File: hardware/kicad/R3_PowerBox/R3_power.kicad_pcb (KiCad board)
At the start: 4 copper layers, 160 x 80 mm, 199 parts, among them J1 SERVICE / BENCH INPUT 6-12V, J10 BATTERY / CHARGER TELEMETRY, J11 USER PANEL / PRIMARY ONLY, J12 PRIMARY B2B 2x8 / DNP, J13 ISOLATED B2B 2x5 / DNP, J2 DIGITAL POWER OUT, J3 ISOLATED POWER OUT, J4 CONTROL / SERVICE, J5 PRIMARY AUX DNP, J6 ISOLATED AUX DNP, J7 USB-C POWER INPUT, J8 2S BATTERY / KEYED / NTC_BMS=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, J9 NTC_CHG=103AT-2 / QUIET DGND 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, Q1 DMP3007LSS-13, Q2 CSD17577Q3AT 30V NMOS DSG, Q3 CSD17577Q3AT 30V NMOS CHG, Q4 DMP3007LSS-13 SYSTEM LOAD SWI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, SW1 C&K RS282G05A3 / POWER ON, SW2 QON SERVICE / TL3305AF160QG, U1 TPS62132RGTR, U10 STUSB4500QTR, U11 BQ294502 SPACE ONLY / NC / DNP, U2 TPS54302DDCR, U3 RS3E-0505S/H3, U4 ADM7150ACPZ-3.3-R7, U5 TPS7A2033PDBVR, U6 RS3-0505D/H3, U7 TPS2121RUXR, U8 BQ25798RQM, U9 BQ28Z610DRZR

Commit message: Route R3 checkpoint E domain planes and thermal returns
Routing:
- net VSYS_MAIN: track 103.1 -> 106.4 mm, vias 5 -> 8
- net GND_ISO: track 24.3 -> 27.3 mm, vias 22 -> 31
- net VSYS_PROT: track 27.9 -> 30.2 mm, vias 3 -> 5
- net DGND: vias 67 -> 85
- added copper zone on B.Cu, net BMS_FET_COMMON
- added copper zone on F.Cu, net BMS_FET_COMMON
- added copper zone on B.Cu, net DGND
- added copper zone on F.Cu, net DGND
- added copper zone on In1.Cu, net DGND
- added copper zone on In2.Cu, net DGND
- added copper zone on B.Cu, net GND_ISO
- added copper zone on F.Cu, net GND_ISO
- added copper zone on In1.Cu, net GND_ISO
- added copper zone on In2.Cu, net GND_ISO
- added copper zone on B.Cu, net VSYS_MAIN
- added copper zone on F.Cu, net VSYS_MAIN
- added copper zone on B.Cu, net VSYS_PROT
- added copper zone on F.Cu, net VSYS_PROT

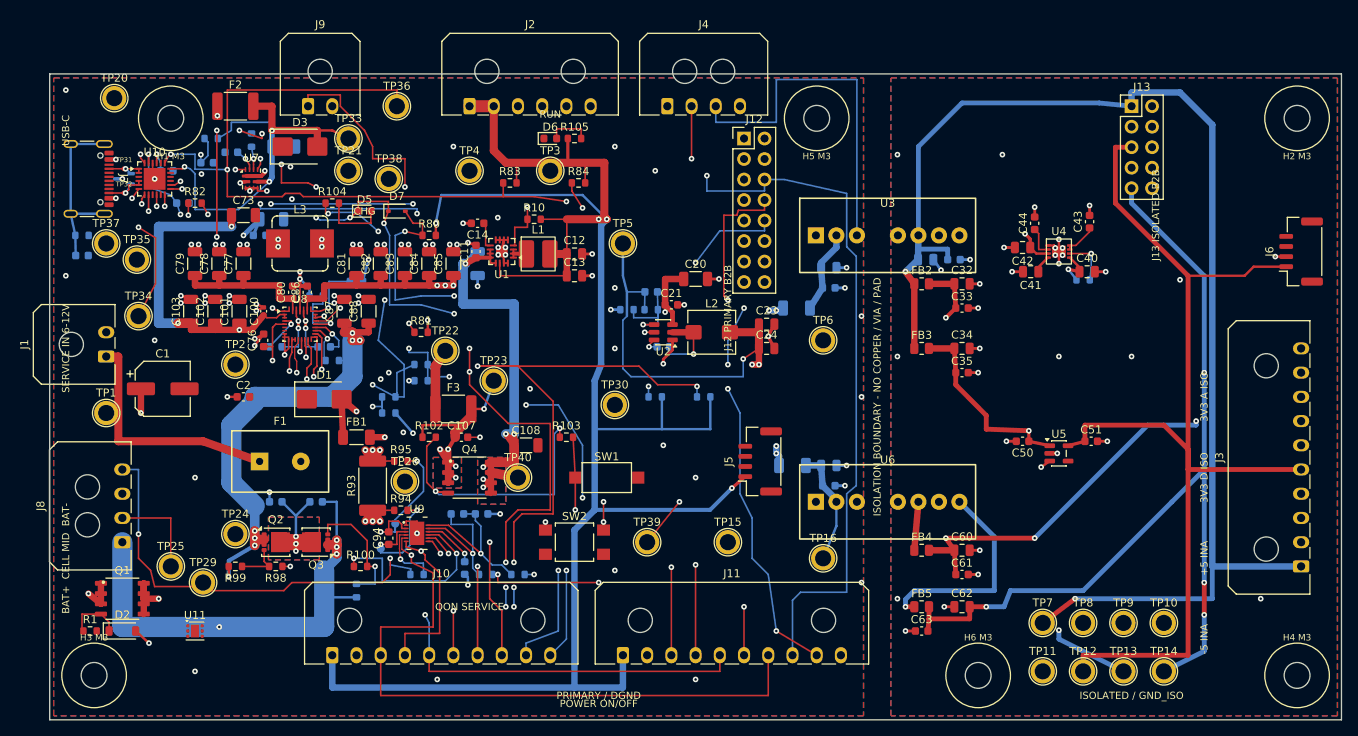
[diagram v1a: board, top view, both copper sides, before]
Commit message: Finish R3 PowerBox routing checkpoint F and verification
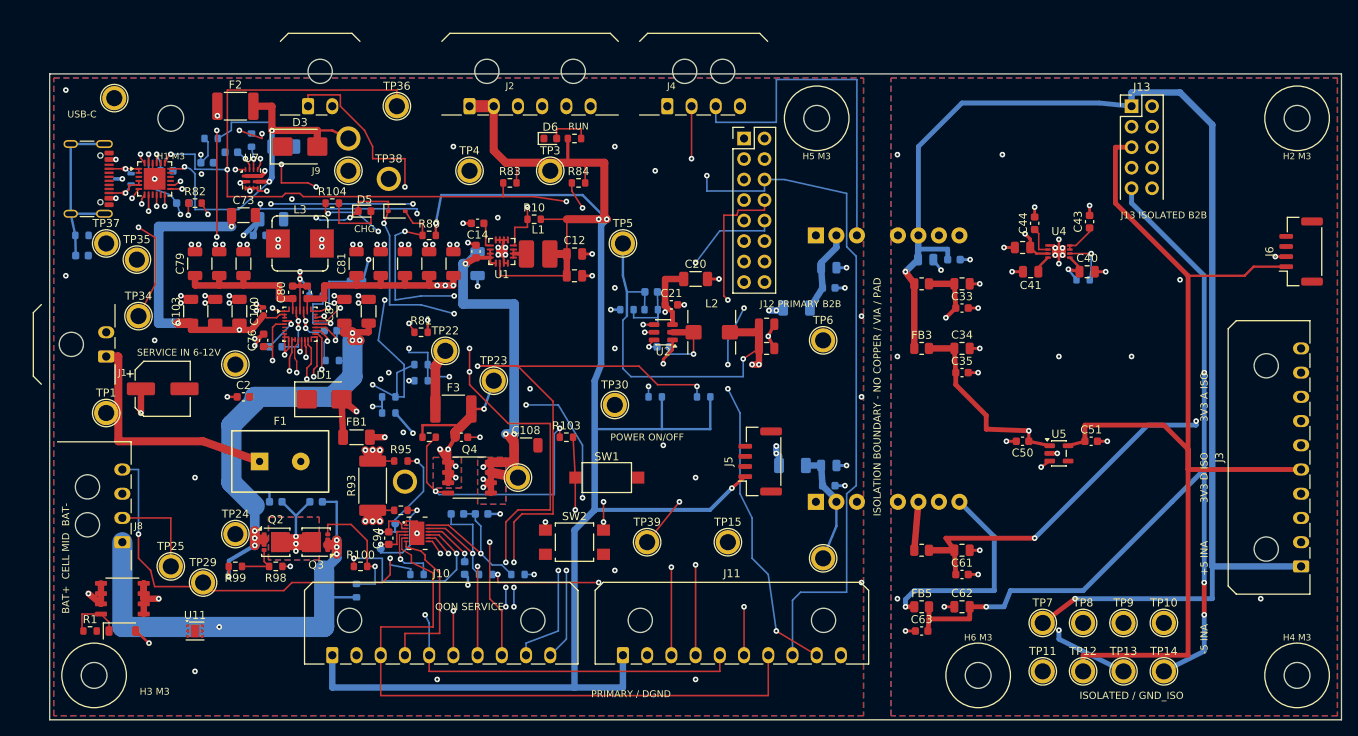
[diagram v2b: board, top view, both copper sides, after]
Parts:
- C1: footprint CP_Elec_6.3x5.8 -> Capacitor_SMD:CP_Elec_6.3x5.8
- C10, C101, C102, C103, C108, C20, C3, C71, C73, C77, C78, C79, C81, C82, C83, C84, C85, C87, C88: footprint C_1206_3216Metric -> Capacitor_SMD:C_1206_3216Metric
- C100: footprint C_0402_1005Metric -> Capacitor_SMD:C_0402_1005Metric
- C104, C105, C106, C107, C11, C14, C2, C21, C22, C25, C27, C29, C31, C33, C35, C4, C43, C44, C50, C51, C61, C63, C70, C72, C74, C75, C76, C80, C86, C89, C93, C94, C95, C96, C97, C98: footprint C_0603_1608Metric -> Capacitor_SMD:C_0603_1608Metric
- C12, C13, C23, C24, C26, C28, C30, C32, C34, C40, C41, C42, C60, C62: footprint C_0805_2012Metric -> Capacitor_SMD:C_0805_2012Metric
- D1, D3: footprint D_SMB -> Diode_SMD:D_SMB
- D2: footprint D_SOD-123 -> Diode_SMD:D_SOD-123
- D4: footprint SOT-323_SC-70 -> Package_TO_SOT_SMD:SOT-323_SC-70
- D5, D6: footprint LED_0603_1608Metric -> LED_SMD:LED_0603_1608Metric
- D7: footprint D_SOD-323 -> Diode_SMD:D_SOD-323
- F1: footprint Fuse_PTC_MF-R250 -> R3_Power:Fuse_PTC_MF-R250
- F2, F3: footprint Fuse_1812_4532Metric_Pad1.30x3.40mm_HandSolder -> Fuse:Fuse_1812_4532Metric_Pad1.30x3.40mm_HandSolder
- FB1, FB6, FB7: footprint L_1206_3216Metric_Pad1.22x1.90mm_HandSolder -> Inductor_SMD:L_1206_3216Metric_Pad1.22x1.90mm_HandSolder
- FB2, FB3, FB4, FB5: footprint R_0805_2012Metric -> Resistor_SMD:R_0805_2012Metric
- J1, J9: footprint Molex_Micro-Fit_3.0_43650-0200_1x02_P3.00mm_Horizontal -> Connector_Molex:Molex_Micro-Fit_3.0_43650-0200_1x02_P3.00mm_Horizontal
- J10, J11, J3: footprint Molex_Micro-Fit_3.0_43650-1000_1x10_P3.00mm_Horizontal -> Connector_Molex:Molex_Micro-Fit_3.0_43650-1000_1x10_P3.00mm_Horizontal
- J12: footprint PinHeader_2x08_P2.54mm_Vertical -> Connector_PinHeader_2.54mm:PinHeader_2x08_P2.54mm_Vertical
- J13: footprint PinHeader_2x05_P2.54mm_Vertical -> Connector_PinHeader_2.54mm:PinHeader_2x05_P2.54mm_Vertical
- J2: footprint Molex_Micro-Fit_3.0_43650-0600_1x06_P3.00mm_Horizontal -> Connector_Molex:Molex_Micro-Fit_3.0_43650-0600_1x06_P3.00mm_Horizontal
- J4, J8: footprint Molex_Micro-Fit_3.0_43650-0400_1x04_P3.00mm_Horizontal -> Connector_Molex:Molex_Micro-Fit_3.0_43650-0400_1x04_P3.00mm_Horizontal
- J5, J6: footprint JST_GH_SM04B-GHS-TB_1x04-1MP_P1.25mm_Horizontal -> Connector_JST:JST_GH_SM04B-GHS-TB_1x04-1MP_P1.25mm_Horizontal
- J7: footprint USB_C_Receptacle_GCT_USB4105-xx-A_16P_TopMnt_Horizontal -> Connector_USB:USB_C_Receptacle_GCT_USB4105-xx-A_16P_TopMnt_Horizontal
- L1: footprint L_Coilcraft_XFL4020 -> R3_Power:L_Coilcraft_XFL4020
- L2: footprint L_Bourns_SRP5030T -> Inductor_SMD:L_Bourns_SRP5030T
- L3: value 1.0uH >=6A / MPN TBD -> SRP7028A-1R0M 1uH; footprint L_Bourns_SRP7028A_7.3x6.6mm -> Inductor_SMD:L_Bourns_SRP7028A_7.3x6.6mm
- Q1, Q4: footprint DMP3007LSS_SO8_LOGICAL -> R3_Power:DMP3007LSS_SO8_LOGICAL
- Q2, Q3: footprint CSD17577Q3A_VSON-8_3.3x3.3mm -> R3_Power:CSD17577Q3A_VSON-8_3.3x3.3mm
- R1, R10, R100, R101, R102, R103, R104, R105, R21, R22, R40, R72, R73, R74, R75, R76, R77, R78, R79, R80, R81, R82, R83, R84, R85, R90, R91, R92, R94, R95, R96, R97, R98, R99: footprint R_0603_1608Metric -> Resistor_SMD:R_0603_1608Metric
- R93: footprint R_2512_6332Metric_Pad1.40x3.35mm_HandSolder -> Resistor_SMD:R_2512_6332Metric_Pad1.40x3.35mm_HandSolder
- SW1: footprint SW_SPST_CK_RS282G05A3 -> Button_Switch_SMD:SW_SPST_CK_RS282G05A3
- SW2: footprint SW_SPST_TL3305A -> Button_Switch_SMD:SW_SPST_TL3305A
- TP1, TP10, TP11, TP12, TP13, TP14, TP15, TP16, TP2, TP20, TP21, TP22, TP23, TP24, TP25, TP26, TP29, TP3, TP30, TP33, TP34, TP35, TP36, TP37, TP38, TP39, TP4, TP40, TP5, TP6, TP7, TP8, TP9: footprint TestPoint_Plated_Hole_D2.0mm -> TestPoint:TestPoint_Plated_Hole_D2.0mm
- TP27, TP28: footprint TestPoint_Pad_D1.0mm -> TestPoint:TestPoint_Pad_D1.0mm
- U1: footprint VQFN-16-1EP_3x3mm_P0.5mm_EP1.45x1.45mm -> Package_DFN_QFN:VQFN-16-1EP_3x3mm_P0.5mm_EP1.45x1.45mm
- U10: footprint QFN-24-1EP_4x4mm_P0.5mm_EP2.7x2.7mm -> Package_DFN_QFN:QFN-24-1EP_4x4mm_P0.5mm_EP2.7x2.7mm
- U11: footprint WSON-6-1EP_2x2mm_P0.65mm_EP1x1.6mm -> Package_SON:WSON-6-1EP_2x2mm_P0.65mm_EP1x1.6mm
- U2: footprint SOT-23-6 -> Package_TO_SOT_SMD:SOT-23-6
- U3: footprint Converter_DCDC_RECOM_RS3E_SIP8 -> R3_Power:Converter_DCDC_RECOM_RS3E_SIP8
- U4: footprint LFCSP-8-1EP_3x3mm_P0.5mm_EP1.74x1.45mm -> R3_Power:LFCSP-8-1EP_3x3mm_P0.5mm_EP1.74x1.45mm
- U5: footprint SOT-23-5 -> Package_TO_SOT_SMD:SOT-23-5
- U6: footprint Converter_DCDC_RECOM_RS3_SIP8 -> R3_Power:Converter_DCDC_RECOM_RS3_SIP8
- U7: footprint Texas_VQFN-HR-12_2x2.5mm_P0.5mm -> Package_DFN_QFN:Texas_VQFN-HR-12_2x2.5mm_P0.5mm
- U8: footprint Texas_RQM0029A_VQFN-29_4x4mm_P0.4mm -> Package_DFN_QFN:Texas_RQM0029A_VQFN-29_4x4mm_P0.4mm
- U9: footprint Texas_DRZ0012A_VSON-12 -> R3_Power:Texas_DRZ0012A_VSON-12
- moved C75 2.15 mm to (54.8, 51.8)
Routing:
- net POWER_CTRL: track 107.3 -> 103.3 mm
- net CHG_SW2: track 19.1 -> 17.8 mm
- net N$8: track 5.43 -> 4.71 mm
- net PM_I2C_SDA: vias 11 -> 10
- net PM_I2C_SCL: vias 10 -> 9
- net PACK_POS: vias 10 -> 9
- net +5V_INA: vias 4 -> 3
- net +3V3_D: vias 7 -> 6

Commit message: Rev.A review fixes: initial schematic and component corrections
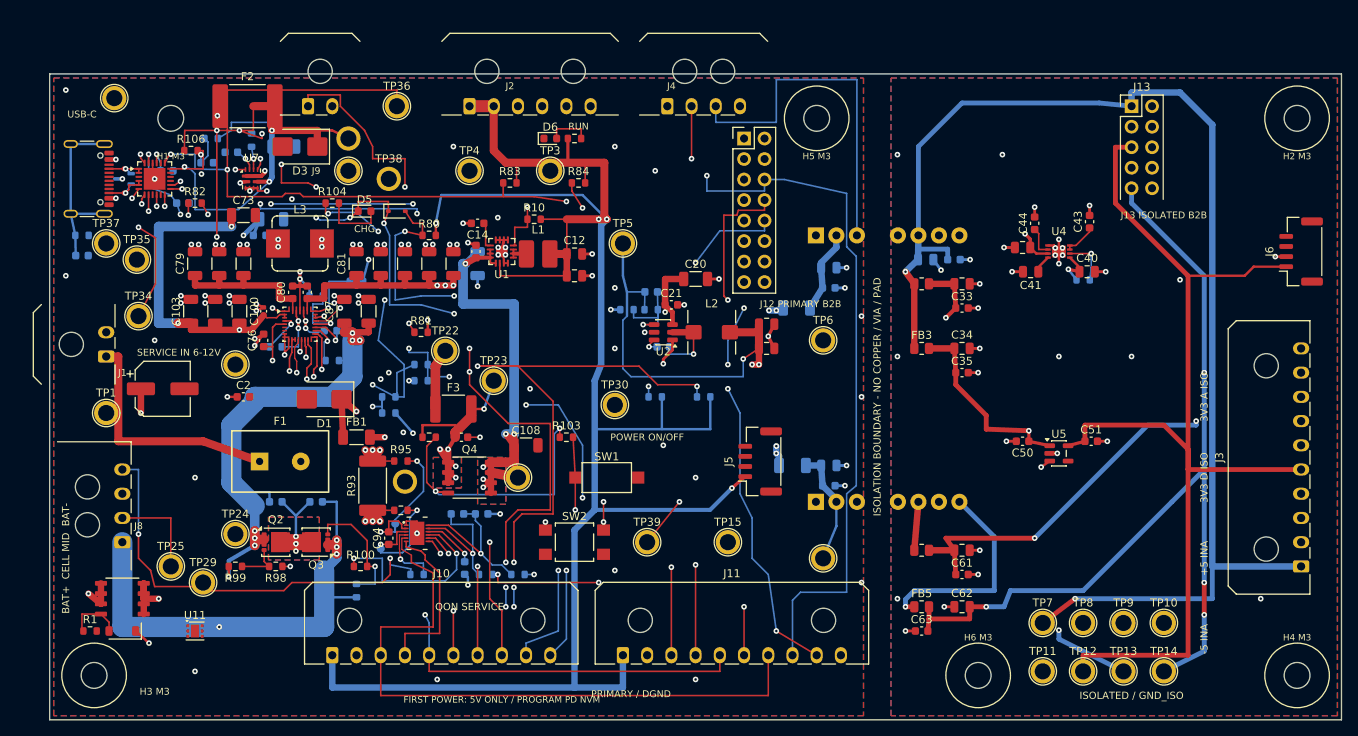
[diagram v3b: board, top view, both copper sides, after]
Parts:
- added R106: 1k VBUS DISCH LIMIT, Resistor_SMD:R_0603_1608Metric, F.Cu at (37.5, 29.5)
- C106: value 4.7uF/25V PD VDD -> 1uF/25V PD VDD
- C71: value 10uF/25V USB -> 4.7uF/25V USB
- C89: value 1nF SDRV -> 1nF/50V C0G SDRV
- F2: value MF-MSMF260/16X-2 2.6A/16V PPTC -> 2920L260/33DR 2.6A/33V; footprint Fuse:Fuse_1812_4532Metric_Pad1.30x3.40mm_HandSolder -> Fuse:Fuse_2920_7451Metric
- FB1: value BLM31PG601SN1 -> BLM31KN121SN1L / 6A
- FB6, FB7: value BLM31KN601B family / 2A -> BLM31KN601SH1L
- J7: value USB-C POWER INPUT -> USB4105-GF-A
- R96, R97: value 10k I2C -> 4.7k I2C
- moved F2 1.50 mm to (44.5, 24.0)
- turned D1 to 180 degrees
- turned D2 to 180 degrees
- turned D3 to 180 degrees
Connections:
- D1 pad 1: DGND -> SERVICE_IN_REV
- D1 pad 2: SERVICE_IN_REV -> DGND
- D2 pad 1: Q1_GATE -> SERVICE_IN_REV
- D2 pad 2: SERVICE_IN_REV -> Q1_GATE
- D3 pad 1: DGND -> USB_VBUS_PROT
- D3 pad 2: USB_VBUS_PROT -> DGND
- U10 pad 18: USB_VBUS_PROT -> PD_VBUS_SENSE_DISCH
- U2 pad 5: VSYS_MAIN -> unconnected-(U2-EN-Pad5)
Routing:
- net USB_VBUS_PROT: track 52.4 -> 67.5 mm
- net PD_VBUS_SENSE_DISCH: track 0.00 -> 6.96 mm
- net VSYS_MAIN: track 106.4 -> 105.2 mm
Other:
- board text added: "FIRST POWER: 5V ONLY / PROGRAM PD NVM"

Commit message: Rev.A review fixes: local charger power-stage reroute checkpoint
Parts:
- added R107: DNP PRELOAD / BENCH SELECT, Resistor_SMD:R_2512_6332Metric, B.Cu at (151.0, 74.0)
- added R108: DNP PRELOAD / BENCH SELECT, Resistor_SMD:R_2512_6332Metric, B.Cu at (153.0, 81.0)
- C23, C24: value 22uF/10V -> 22uF/25V GRM32ER71E226KE15L; footprint Capacitor_SMD:C_0805_2012Metric -> Capacitor_SMD:C_1210_3225Metric
- C40: value 10uF VIN -> 22uF/25V GRM32ER71E226KE15L; footprint Capacitor_SMD:C_0805_2012Metric -> Capacitor_SMD:C_1210_3225Metric
- C41: value 10uF VREG -> 22uF/25V GRM32ER71E226KE15L; footprint Capacitor_SMD:C_0805_2012Metric -> Capacitor_SMD:C_1210_3225Metric
- C42: value 10uF VOUT -> 22uF/25V GRM32ER71E226KE15L; footprint Capacitor_SMD:C_0805_2012Metric -> Capacitor_SMD:C_1210_3225Metric
- F2, R106: moved to B.Cu
- FB4: value FB_INA_P / FB-or-0R -> 0R / FB / L BENCH SELECT; footprint Resistor_SMD:R_0805_2012Metric -> Inductor_SMD:L_1206_3216Metric_Pad1.22x1.90mm_HandSolder
- FB5: value FB_INA_N / FB-or-0R -> 0R / FB / L BENCH SELECT; footprint Resistor_SMD:R_0805_2012Metric -> Inductor_SMD:L_1206_3216Metric_Pad1.22x1.90mm_HandSolder
- moved C77 4.28 mm to (46.6, 46.9), turned to 180 degrees
- moved R106 4.10 mm to (37.5, 33.6), turned to 90 degrees
- moved C81 3.94 mm to (56.0, 46.9), turned to 0 degrees
- moved R40 2.00 mm to (148.0, 47.5)
- moved C44 1.50 mm to (142.0, 37.0)
- moved C87 1.48 mm to (57.2, 50.7)
- moved C40 1.22 mm to (149.5, 45.2)
- moved C41 1.22 mm to (140.5, 45.2)
- moved C100 1.00 mm to (47.5, 49.4)
- moved C24 1.00 mm to (108.8, 55.0)
- moved FB4 1.00 mm to (128.0, 80.0)
- moved L3 1.00 mm to (51.0, 42.0)
- moved F2 0.86 mm to (43.8, 23.5)
- moved C101 0.80 mm to (42.7, 49.4)
- moved C42 0.71 mm to (140.0, 41.0)
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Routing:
- net USB_VBUS_PROT: track 67.5 -> 45.6 mm, vias 3 -> 2
- net USB_VBUS_RAW: track 35.7 -> 44.2 mm
- net VSYS_MAIN: track 105.2 -> 101.6 mm, vias 8 -> 7
- net +5V_ISO_A: track 80.6 -> 83.9 mm
- net GND_ISO: track 27.3 -> 24.4 mm, vias 31 -> 33
- net PD_VBUS_SENSE_DISCH: track 6.96 -> 4.09 mm, vias 0 -> 1
- net VSYS_RAW: track 45.0 -> 47.1 mm
- net EN_3V3_A_ISO: track 5.91 -> 7.90 mm
- net N$14: track 3.83 -> 5.42 mm, vias 0 -> 2
- net +5V_INA: track 117.8 -> 119.0 mm
- net PACK_POS: track 115.7 -> 114.5 mm
- net -5V_INA: track 126.9 -> 128.1 mm
- net CHG_PMID: track 18.9 -> 20.0 mm
- net +5V_INA_RAW: track 6.02 -> 7.11 mm
- net DGND: track 101.5 -> 100.4 mm, vias 85 -> 89
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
